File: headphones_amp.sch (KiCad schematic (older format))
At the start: 44 parts, among them P1 INPUTS, P2 POWER, P3 OUPUTS, Q1 Q_NPN_EBC, Q2 Q_PNP_EBC, Q3 Q_NPN_EBC, Q4 Q_PNP_EBC, U1 MC33178

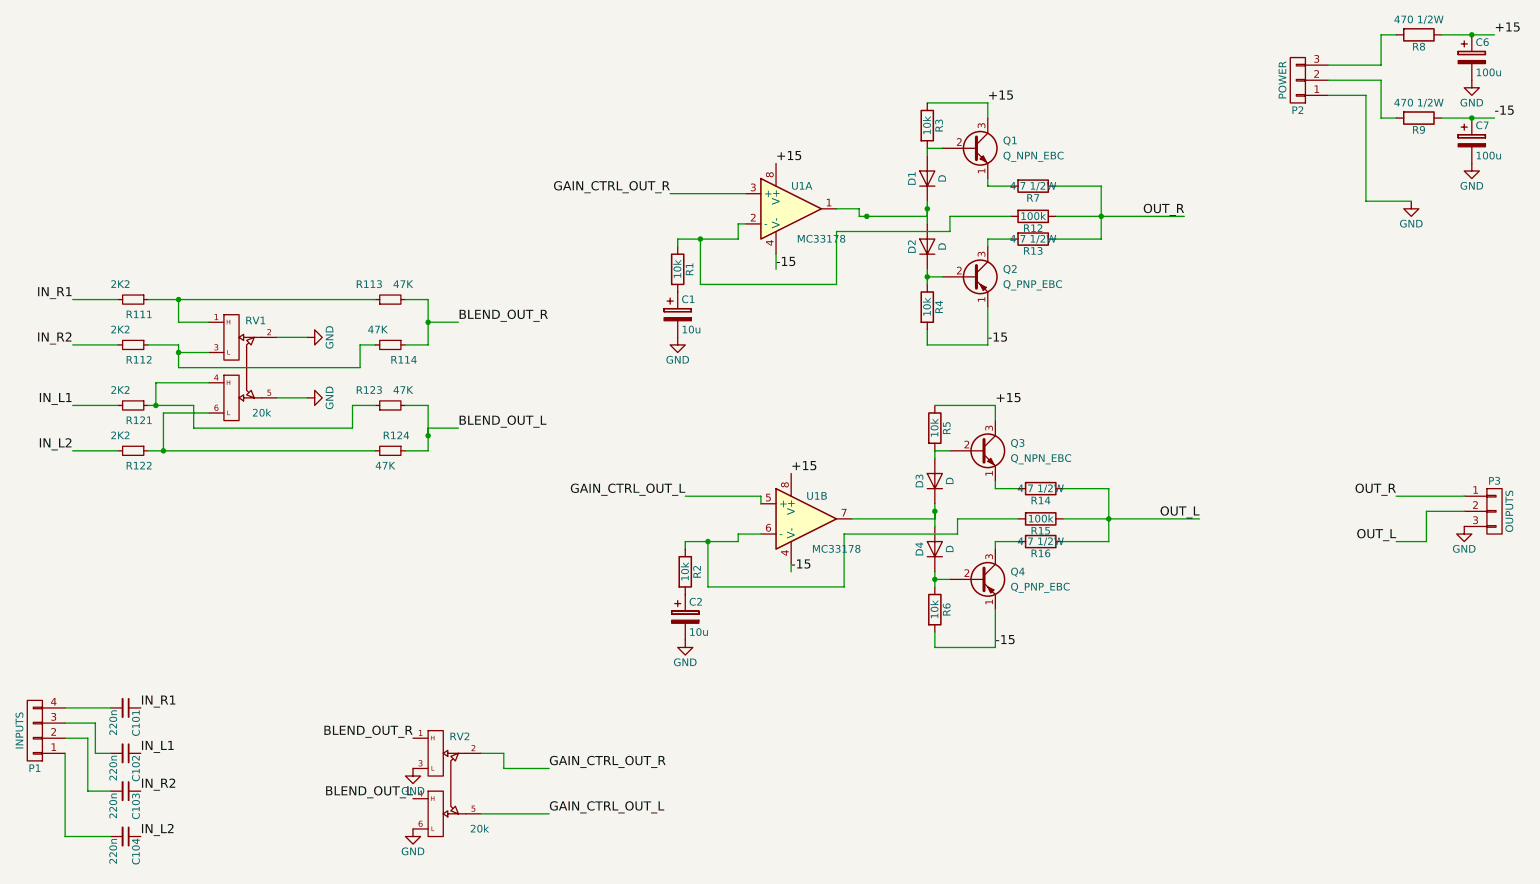
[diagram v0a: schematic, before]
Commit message: Updated components references
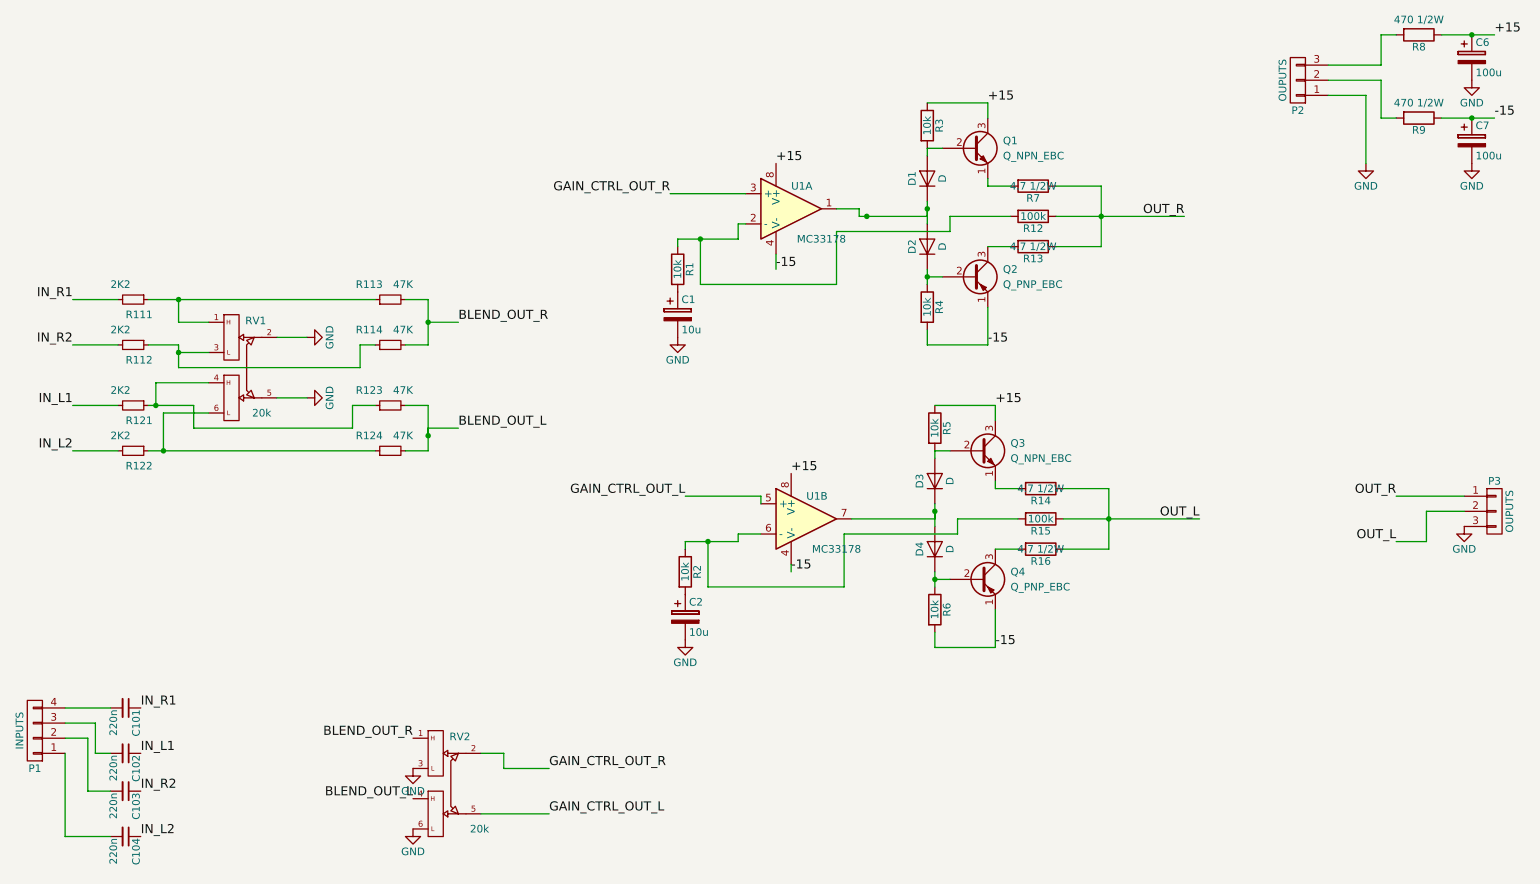
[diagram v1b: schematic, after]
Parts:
- C1, C2: Mfg_Part_# (none) -> 0; Package 0402 -> 2-THT
- C101, C102, C103, C104: Mfg_Part_# (none) -> R82EC3220Z370J
- C6, C7: Mfg_Part_# (none) -> ULD1E101MED1TD; Package 0402 -> 2-THT
- D1, D2, D3, D4: Mfg_Part_# (none) -> 1N4148
- P1: Description (none) -> Embases et logements de câbles WR-PHD 2.54mm Hdr 4P Single 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; Distributor Digikey -> Mouser; Distributor Part # (none) -> 710-61300411021; Manufacturer (none) -> Wurth Electronics; Mfg_Part_# (none) -> 61300411021; Mfg_Part_No 0 -> 61300411021; Package 0402 -> 4-THT
- P2: value POWER -> OUPUTS; Description (none) -> Embases et logements de câbles WR-PHD 2.54mm Hdr 3P Single 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; Distributor (none) -> Mouser; Distributor Part # (none) -> 710-61300311021; Manufacturer (none) -> Wurth Electronics; Mfg_Part_# (none) -> 61300311021; Mfg_Part_No (none) -> 61300311021; Package (none) -> 3-THT
- P3: Description (none) -> Embases et logements de câbles WR-PHD 2.54mm Hdr 3P Single 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; Distributor Digikey -> Mouser; Distributor Part # (none) -> 710-61300311021; Manufacturer (none) -> Wurth Electronics; Mfg_Part_# (none) -> 61300311021; Mfg_Part_No 0 -> 61300311021; Package 0402 -> 3-THT
- Q1, Q3: Description (none) -> Transistors bipolaires - BJT NPN Silicon; Manufacturer Central -> Central Semiconductor; Mfg_Part_# (none) -> 2N2222
- Q2, Q4: Description (none) -> Transistors bipolaires - BJT PNP Silicon; Manufacturer Central -> Central Semiconductor; Mfg_Part_# (none) -> 2N2907A
- R1, R2, R3, R4, R5, R6: Description (none) -> Résistances à couche métallique - Trou traversant 1/3watts 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; Distributor (none) -> Mouser; Distributor Part # (none) -> 71-CCF5010K0FKE36; Manufacturer (none) -> Vishay / Dale; Mfg_Part_# (none) -> CCF5010K0FKE36; Package (none) -> DIN0204
- R111, R112, R121, R122: Description (none) -> Résistances à couche mince - Trou traversant .4watt 2.2Kohm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; Distributor (none) -> Mouser; Distributor Part # (none) -> 594-5063JD2K200F; Manufacturer (none) -> Vishay / BC Components; Mfg_Part_# (none) -> MBA02040C2201FC100; Package (none) -> 2-THT
- R113, R114, R123, R124: Description (none) -> Résistances à couche mince - Trou traversant .4watt 47Kohms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; Distributor (none) -> Mouser; Distributor Part # (none) -> 594-5063JD47K00F; Manufacturer (none) -> Vishay / BC Components; Mfg_Part_# (none) -> MBA02040C4702FC100; Package (none) -> 1.6 mm x 3.6 mm
- R12, R15: Description (none) -> Résistances à couche métallique - Trou traversant 1/3watts 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; Distributor (none) -> Mouser; Distributor Part # (none) -> 71-CCF50-100K; Manufacturer (none) -> Vishay / Dale; Mfg_Part_# (none) -> CCF50100KFKR36; Package (none) -> DIN0204
- R13, R14, R16, R7: footprint Resistors_ThroughHole:R_Axial_DIN0204_L3.6mm_D1.6mm_P5.08mm_Horizontal -> Resistors_THT:R_Axial_DIN0207_L6.3mm_D2.5mm_P10.16mm_Horizontal; Description (none) -> Résistances à couche métallique - Trou traversant 1/2W 4.7K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; Distributor (none) -> Mouser; Distributor Part # (none) -> 71-CMF554K7000FKR6; Manufacturer (none) -> Vishay / Dale; Mfg_Part_# (none) -> CMF554K7000FKR6; Package (none) -> DIN0207
- R8, R9: footprint Resistors_ThroughHole:Resistor_Horizontal_RM7mm -> Resistors_THT:R_Axial_DIN0207_L6.3mm_D2.5mm_P10.16mm_Horizontal; Description (none) -> Résistances à couche métallique - Trou traversant 1/2watt 4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; Distributor (none) -> Mouser; Distributor Part # (none) -> 594-SFR25H0004700FR5; Manufacturer (none) -> Vishay / BC Components; Mfg_Part_# (none) -> SFR25H0004700FR500; Package (none) -> DIN0207
- RV1: Mfg_Part_# (none) -> RK0971210Z2M
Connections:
- net BLEND_OUT_L: now also R124.2; no longer R124.1
- net BLEND_OUT_R: now also R114.2; no longer R114.1
- net at R112.1, RV1.3: now also R114.1; no longer R114.2
- net at R122.1, RV1.6: now also R124.1; no longer R124.2
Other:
- moved on the sheet: R13

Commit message: Add missing references
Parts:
- RV2: Mfg_Part_# (none) -> RK09712200HA
- U1: Description (none) -> Amplificateurs opérationnels - Amplis-Op Dual Low Noise; Distributor (none) -> Mouser; Distributor Part # (none) -> 595-NE5532P; Manufacturer (none) -> Texas Instruments; Mfg_Part_# (none) -> NE5532P; Package (none) -> 8-PDIP
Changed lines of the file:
@@
 $EndComp
 $Comp
-L GND #PWR109
+L GND #PWR01
 U 1 1 56CD0B36
 P 10200 1150
-F 0 "#PWR109" H 10200 900 50  0001 C CNN
+F 0 "#PWR01" H 10200 900 50  0001 C CNN
 F 1 "GND" H 10200 1000 50  0000 C CNN
 F 2 "" H 10200 1150 50  0000 C CNN
@@
 $EndComp
 $Comp
-L GND #PWR110
+L GND #PWR02
 U 1 1 56CD0C14
 P 10200 1700
-F 0 "#PWR110" H 10200 1450 50  0001 C CNN
+F 0 "#PWR02" H 10200 1450 50  0001 C CNN
 F 1 "GND" H 10200 1550 50  0000 C CNN
 F 2 "" H 10200 1700 50  0000 C CNN
@@
 $EndComp
 $Comp
-L GND #PWR107
+L GND #PWR03
 U 1 1 56CD0CC7
 P 9500 1700
-F 0 "#PWR107" H 9500 1450 50  0001 C CNN
+F 0 "#PWR03" H 9500 1450 50  0001 C CNN
 F 1 "GND" H 9500 1550 50  0000 C CNN
 F 2 "" H 9500 1700 50  0000 C CNN
@@
 BLEND_OUT_L
 $Comp
-L GND #PWR103
+L GND #PWR04
 U 1 1 56CDC6F6
 P 3200 5700
-F 0 "#PWR103" H 3200 5450 50  0001 C CNN
+F 0 "#PWR04" H 3200 5450 50  0001 C CNN
 F 1 "GND" H 3200 5550 50  0000 C CNN
 F 2 "" H 3200 5700 50  0000 C CNN
@@
 $EndComp
 $Comp
-L GND #PWR104
+L GND #PWR05
 U 1 1 56CDC74C
 P 3200 6100
-F 0 "#PWR104" H 3200 5850 50  0001 C CNN
+F 0 "#PWR05" H 3200 5850 50  0001 C CNN
 F 1 "GND" H 3200 5950 50  0000 C CNN
 F 2 "" H 3200 6100 50  0000 C CNN
@@
 -15
 $Comp
-L GND #PWR106
+L GND #PWR06
 U 1 1 570A4701
 P 5000 4850
-F 0 "#PWR106" H 5000 4600 50  0001 C CNN
+F 0 "#PWR06" H 5000 4600 50  0001 C CNN
 F 1 "GND" H 5000 4700 50  0000 C CNN
 F 2 "" H 5000 4850 50  0000 C CNN
@@
 $EndComp
 $Comp
-L GND #PWR105
+L GND #PWR07
 U 1 1 570A4CB5
 P 4950 2850
-F 0 "#PWR105" H 4950 2600 50  0001 C CNN
+F 0 "#PWR07" H 4950 2600 50  0001 C CNN
 F 1 "GND" H 4950 2700 50  0000 C CNN
 F 2 "" H 4950 2850 50  0000 C CNN
@@
 Text Label 9700 3900 2    60   ~ 0
 OUT_R
-$Comp
-L MC33178 U1
-U 1 1 5709814B
-P 5700 2000
-F 0 "U1" H 5700 2150 50  0000 L CNN
-F 1 "MC33178" H 5900 1800 50  0000 C CNN
-F 2 "Housings_DIP:DIP-8_W7.62mm_LongPads" H 5600 2050 50  0001 C CNN
-F 3 "" H 5700 2150 50  0000 C CNN
-	1    5700 2000
-	1    0    0    -1
-$EndComp
 $Comp
 L MC33178 U1
@@
 F 1 "MC33178" H 6000 3850 50  0000 C CNN
 F 2 "Housings_DIP:DIP-8_W7.62mm_LongPads" H 5700 4100 50  0001 C CNN
-F 3 "" H 5800 4200 50  0000 C CNN
+F 3 "http://www.ti.com/lit/gpn/ne5532" H 5800 4200 50  0001 C CNN
+F 4 "NE5532P" H 5800 4050 60  0001 C CNN "Mfg_Part_#"
+F 5 "Mouser" H 5800 4050 60  0001 C CNN "Distributor"
+F 6 "595-NE5532P" H 5800 4050 60  0001 C CNN "Distributor Part #"
+F 7 "8-PDIP" H 5800 4050 60  0001 C CNN "Package"
+F 8 "Amplificateurs opérationnels - Amplis-Op Dual Low Noise" H 5800 4050 60  0001 C CNN "Description"
+F 9 "Texas Instruments" H 5800 4050 60  0001 C CNN "Manufacturer"
 	2    5800 4050
 	1    0    0    -1
@@
 $EndComp
 $Comp
-L GND #PWR108
+L GND #PWR08
 U 1 1 575F8D25
 P 10150 4100
-F 0 "#PWR108" H 10150 3850 50  0001 C CNN
+F 0 "#PWR08" H 10150 3850 50  0001 C CNN
 F 1 "GND" H 10150 3950 50  0000 C CNN
 F 2 "" H 10150 4100 50  0000 C CNN
@@
 $EndComp
 Wire Wire Line
-	7450 2050 7750 2050
-Wire Wire Line
-	7750 2050 8300 2050
+	7450 2050 8300 2050
 Wire Wire Line
 	3650 6000 4100 6000
@@
 	5000 3900 5500 3900
 Wire Wire Line
-	6600 2050 6200 2050
-Wire Wire Line
-	6200 2050 6150 2050
-Wire Wire Line
-	6600 1950 6600 2000
-Wire Wire Line
-	6600 2000 6600 2050
+	6600 2050 6150 2050
+Wire Wire Line
+	6600 1950 6600 2050
 Wire Wire Line
 	6600 2100 6600 2000
 Connection ~ 6600 2000
 Wire Wire Line
-	6600 2400 6600 2450
-Wire Wire Line
-	6600 2450 6600 2500
+	6600 2400 6600 2500
 Wire Wire Line
 	6600 2450 6700 2450
@@
 	7450 1850 7750 1850
 Wire Wire Line
-	7750 1850 7750 2050
-Wire Wire Line
-	7750 2050 7750 2250
+	7750 1850 7750 2250
 Wire Wire Line
 	7750 2250 7450 2250
@@
 	5100 2500 5100 2200
 Wire Wire Line
-	4950 2200 5100 2200
-Wire Wire Line
-	5100 2200 5350 2200
+	4950 2200 5350 2200
 Wire Wire Line
 	4950 2200 4950 2250
 Connection ~ 5100 2200
 Wire Wire Line
-	7000 2250 7000 2250
-Wire Wire Line
 	7000 2250 7150 2250
 Wire Wire Line
-	7500 4050 7800 4050
-Wire Wire Line
-	7800 4050 8400 4050
+	7500 4050 8400 4050
 Wire Wire Line
 	6650 4050 6100 4050
 Wire Wire Line
-	6650 3950 6650 4000
-Wire Wire Line
-	6650 4000 6650 4050
+	6650 3950 6650 4050
 Wire Wire Line
 	6650 4100 6650 4000
 Connection ~ 6650 4000
 Wire Wire Line
-	6650 4400 6650 4450
-Wire Wire Line
-	6650 4450 6650 4500
+	6650 4400 6650 4500
 Wire Wire Line
 	6650 4450 6750 4450
@@
 	7500 3850 7800 3850
 Wire Wire Line
-	7800 3850 7800 4050
-Wire Wire Line
-	7800 4050 7800 4250
+	7800 3850 7800 4250
 Wire Wire Line
 	7800 4250 7500 4250
@@
 	6800 4150 6050 4150
 Wire Wire Line
-	7050 4250 7050 4250
-Wire Wire Line
 	7050 4250 7200 4250
 Wire Wire Line
@@
 	6050 4500 6050 4150
 Wire Wire Line
-	5000 4200 5150 4200
-Wire Wire Line
-	5150 4200 5350 4200
+	5000 4200 5350 4200
 Wire Wire Line
 	5000 4200 5000 4250
@@
 	9600 850  9700 850
 Wire Wire Line
-	10000 850  10200 850
-Wire Wire Line
-	10200 850  10350 850
+	10000 850  10350 850
 Connection ~ 10200 850
 Wire Wire Line
 	9600 1400 9700 1400
 Wire Wire Line
-	10000 1400 10200 1400
-Wire Wire Line
-	10200 1400 10350 1400
+	10000 1400 10350 1400
 Wire Wire Line
 	5600 2400 5600 2300
@@
 	1250 2600 950  2600
 $Comp
-L GND #PWR101
+L GND #PWR09
 U 1 1 576A9EFE
 P 2500 2850
-F 0 "#PWR101" H 2500 2600 50  0001 C CNN
+F 0 "#PWR09" H 2500 2600 50  0001 C CNN
 F 1 "GND" H 2500 2700 50  0000 C CNN
 F 2 "" H 2500 2850 50  0000 C CNN
@@
 $EndComp
 $Comp
-L GND #PWR102
+L GND #PWR010
 U 1 1 576AA7B7
 P 2500 3250
-F 0 "#PWR102" H 2500 3000 50  0001 C CNN
+F 0 "#PWR010" H 2500 3000 50  0001 C CNN
 F 1 "GND" H 2500 3100 50  0000 C CNN
 F 2 "" H 2500 3250 50  0000 C CNN
@@
 	3150 2600 3300 2600
 Wire Wire Line
-	3300 2600 3300 2750
-Wire Wire Line
-	3300 2750 3300 2900
+	3300 2600 3300 2900
 Wire Wire Line
 	3300 2900 3150 2900
@@
 	3150 3300 3300 3300
 Wire Wire Line
-	3300 3300 3300 3500
-Wire Wire Line
-	3300 3500 3300 3600
+	3300 3300 3300 3600
 Wire Wire Line
 	3300 3600 3150 3600
@@
 	1450 2900 1650 2900
 Wire Wire Line
-	1650 2900 1650 2950
-Wire Wire Line
-	1650 2950 1650 3050
+	1650 2900 1650 3050
 Wire Wire Line
 	1650 2950 1850 2950
@@
 	1550 3350 1550 3600
 Wire Wire Line
-	1450 3600 1550 3600
-Wire Wire Line
-	1550 3600 2950 3600
-Wire Wire Line
-	1450 2600 1650 2600
-Wire Wire Line
-	1650 2600 2950 2600
+	1450 3600 2950 3600
+Wire Wire Line
+	1450 2600 2950 2600
 Connection ~ 1650 2600
 Wire Wire Line
@@
 	2800 3450 1750 3450
 Wire Wire Line
-	1750 3450 1750 3300
+	1750 3300 1750 3450
 Connection ~ 1550 3600
 Wire Wire Line
 	1500 3150 1500 3300
 Wire Wire Line
-	1750 3300 1500 3300
-Wire Wire Line
-	1500 3300 1450 3300
+	1450 3300 1750 3300
 Wire Wire Line
 	1500 3150 1850 3150
@@
 F 1 "20k" H 3640 5500 50  0000 C CNN
 F 2 "ALPS_pot:Potentiometer_ALPS_RK097" H 3350 5800 50  0001 C CNN
-F 3 "" H 3350 5800 50  0000 C CNN
-F 4 "RK09712200HA" H 3350 5800 60  0001 C CNN "Mfg_Part_No"
-F 5 "Potentiometers 10 KOhms 30%" H 3350 5800 60  0001 C CNN "Description"
-F 6 "ALPS" H 3350 5800 60  0001 C CNN "Manufacturer"
-F 7 "Mouser" H 3350 5800 60  0001 C CNN "Distributor"
-F 8 "688-RK09712200HA" H 3350 5800 60  0001 C CNN "Distributor Part #"
-F 9 "ALPS_RK097" H 3350 5800 60  0001 C CNN "Package"
+F 3 "http://www.alps.com/WebObjects/catalog.woa/E/HTML/Potentiometer/RotaryPotentiometers/RK097/RK09712200HA.html" H 3350 5800 50  0001 C CNN
+F 4 "RK09712200HA" H 3350 5800 60  0001 C CNN "Mfg_Part_#"
+F 5 "Mouser" H 3350 5800 60  0001 C CNN "Distributor"
+F 6 "688-RK09712200HA" H 3350 5800 60  0001 C CNN "Distributor Part #"
+F 7 "ALPS_RK097" H 3350 5800 60  0001 C CNN "Package"
+F 8 "Potentiometers 10 KOhms 30%" H 3350 5800 60  0001 C CNN "Description"
+F 9 "ALPS" H 3350 5800 60  0001 C CNN "Manufacturer"
+F 10 "RK09712200HA" H 3350 5800 60  0001 C CNN "Mfg_Part_No"
 	1    3350 5800
 	1    0    0    -1
@@
 	0    1    1    0
 $EndComp
+$Comp
+L MC33178 U1
+U 1 1 5A0EE68A
+P 5700 2000
+F 0 "U1" H 5700 2150 50  0000 L CNN
+F 1 "MC33178" H 5900 1800 50  0000 C CNN
+F 2 "Housings_DIP:DIP-8_W7.62mm_LongPads" H 5600 2050 50  0001 C CNN
+F 3 "http://www.ti.com/lit/gpn/ne5532" H 5700 2150 50  0001 C CNN
+F 4 "NE5532P" H 5700 2000 60  0001 C CNN "Mfg_Part_#"
+F 5 "Mouser" H 5700 2000 60  0001 C CNN "Distributor"
+F 6 "595-NE5532P" H 5700 2000 60  0001 C CNN "Distributor Part #"
+F 7 "8-PDIP" H 5700 2000 60  0001 C CNN "Package"
+F 8 "Amplificateurs opérationnels - Amplis-Op Dual Low Noise" H 5700 2000 60  0001 C CNN "Description"
+F 9 "Texas Instruments" H 5700 2000 60  0001 C CNN "Manufacturer"
+	1    5700 2000
+	1    0    0    -1
+$EndComp
 $EndSCHEMATC

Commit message: Add missing references
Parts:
- C1, C2: Mfg_Part_# 0 -> USR1V100MDD1TE
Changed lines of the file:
@@
 F 2 "w_capacitors:CP_5x11mm" H 4988 2550 50  0001 C CNN
 F 3 "http://www.mouser.com/ds/2/293/e-usa_usr-880000.pdf" H 4950 2700 50  0001 C CNN
-F 4 "0" H 4950 2700 60  0001 C CNN "Mfg_Part_#"
+F 4 "USR1V100MDD1TE" H 4950 2700 60  0001 C CNN "Mfg_Part_#"
 F 5 "Mouser" H 4950 2700 60  0001 C CNN "Distributor"
 F 6 "647-USR1V100MDD1TE" H 4950 2700 60  0001 C CNN "Distributor Part #"
@@
 	2800 3450 1750 3450
 Wire Wire Line
-	1750 3300 1750 3450
+	1750 3450 1750 3300
 Connection ~ 1550 3600
 Wire Wire Line
 	1500 3150 1500 3300
 Wire Wire Line
-	1450 3300 1750 3300
+	1750 3300 1450 3300
 Wire Wire Line
 	1500 3150 1850 3150
@@
 F 2 "w_capacitors:CP_5x11mm" H 5038 4550 50  0001 C CNN
 F 3 "http://www.mouser.com/ds/2/293/e-usa_usr-880000.pdf" H 5000 4700 50  0001 C CNN
-F 4 "0" H 5000 4700 60  0001 C CNN "Mfg_Part_#"
+F 4 "USR1V100MDD1TE" H 5000 4700 60  0001 C CNN "Mfg_Part_#"
 F 5 "Mouser" H 5000 4700 60  0001 C CNN "Distributor"
 F 6 "647-USR1V100MDD1TE" H 5000 4700 60  0001 C CNN "Distributor Part #"
